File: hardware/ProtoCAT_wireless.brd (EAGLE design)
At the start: 59.7 x 53.3 mm, 67 parts, among them Q1 MOSFET-NCHANNELSMD, Q2 MOSFET-NCHANNELSMD, U1 ARDUINO, U3 TB6612FNG

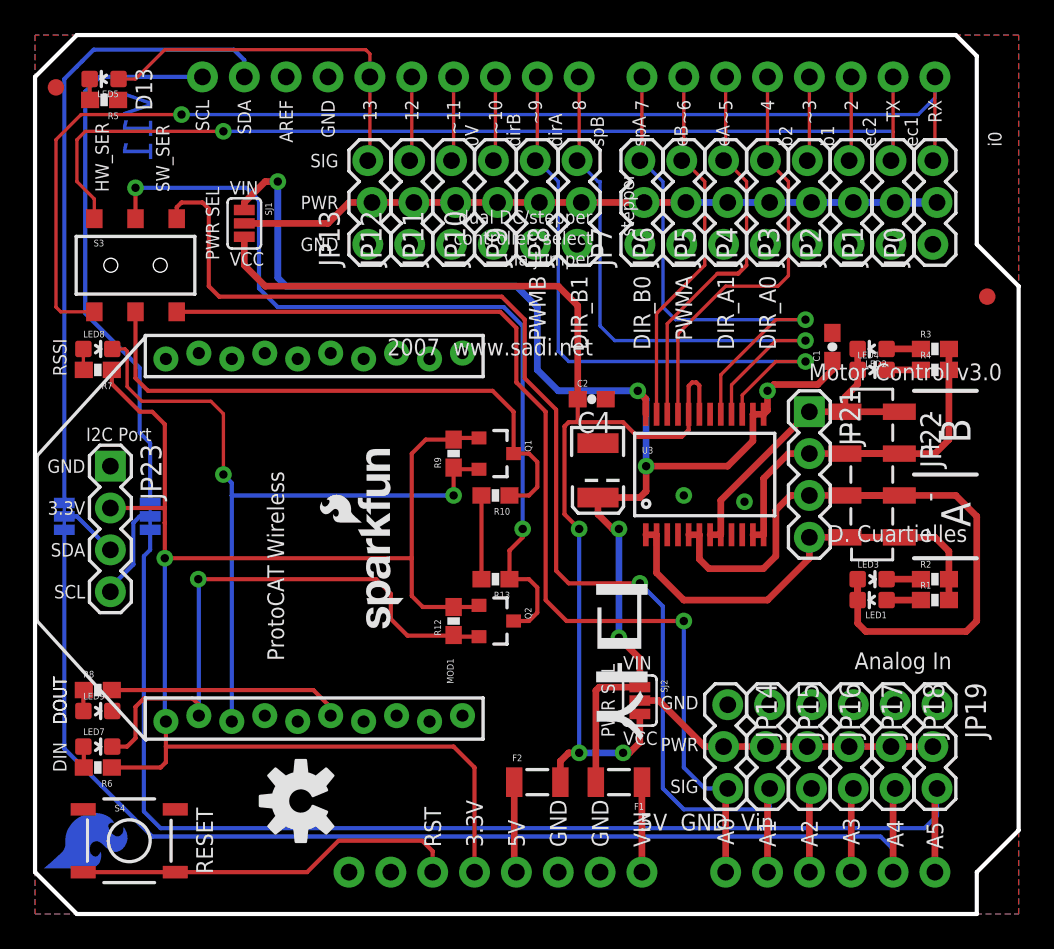
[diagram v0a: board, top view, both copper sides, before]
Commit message: Updated XBee footprint and added RESET control
Added RESET for XBee and fixed PWR lines to the XBee
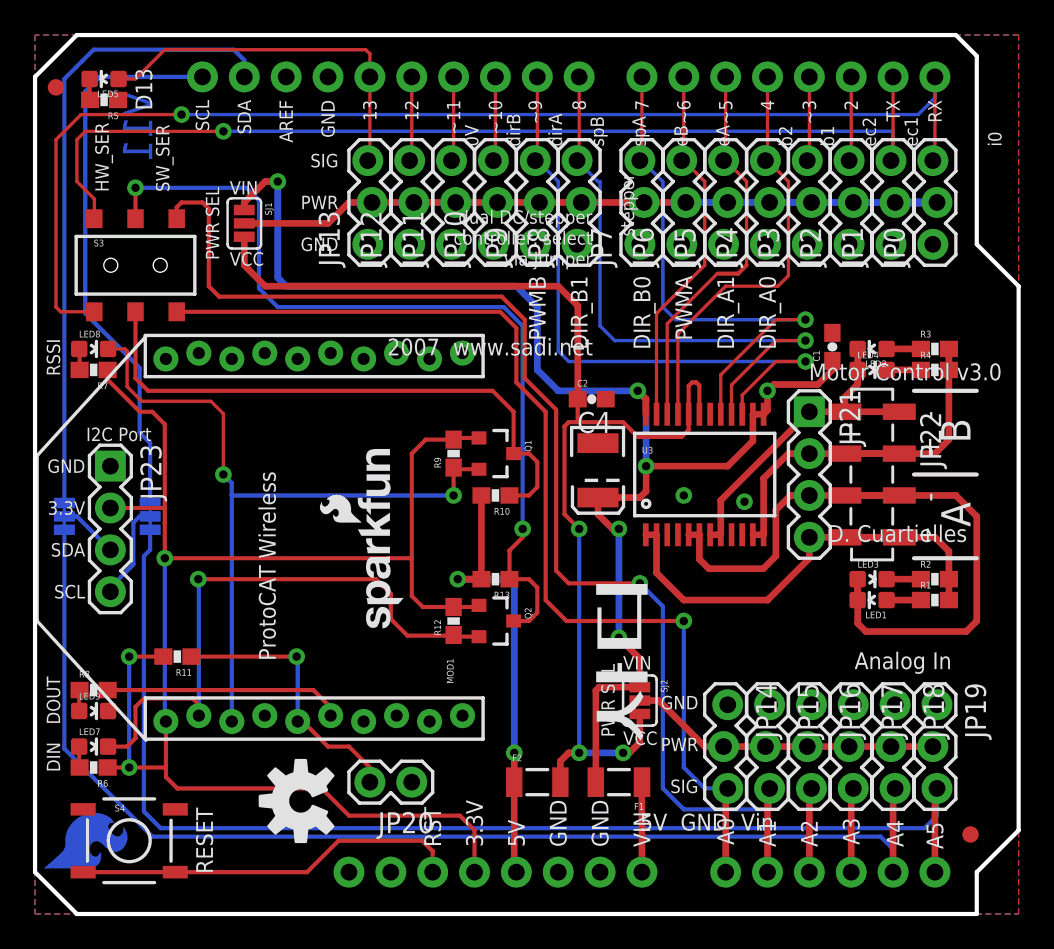
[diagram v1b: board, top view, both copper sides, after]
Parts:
- added JP20: M02PTH, SparkFun-Connectors:1X02
- added R11: 1k, SparkFun-Resistors:0603-RES
- moved FID2 32.7 mm to (56.8, 4.83)
- moved LED7 0.25 mm to (3.56, 10.2)
- moved LED8 0.25 mm to (3.56, 34.3)
- moved LED9 0.25 mm to (3.56, 12.3)
- moved R6 0.25 mm to (3.56, 8.89)
- moved R7 0.25 mm to (3.56, 33.0)
- moved R8 0.25 mm to (3.56, 13.6)
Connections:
- removed net 5V: R10.2, R13.2
- net 3.3V: now also R11.2
- net GND: now also JP20.1
- net VCC: now also R10.2, R13.2
- net XBEE_RESET: now also JP20.2, R11.1
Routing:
- net VCC: track 5.51 -> 27.6 mm, vias 0 -> 2
- net XBEE_RESET: track 0.00 -> 16.8 mm, vias 0 -> 1
- net 3.3V: track 90.5 -> 97.4 mm, vias 1 -> 3
- net 5V: track 5.08 -> 0.00 mm
